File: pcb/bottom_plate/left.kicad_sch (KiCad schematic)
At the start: 18 parts

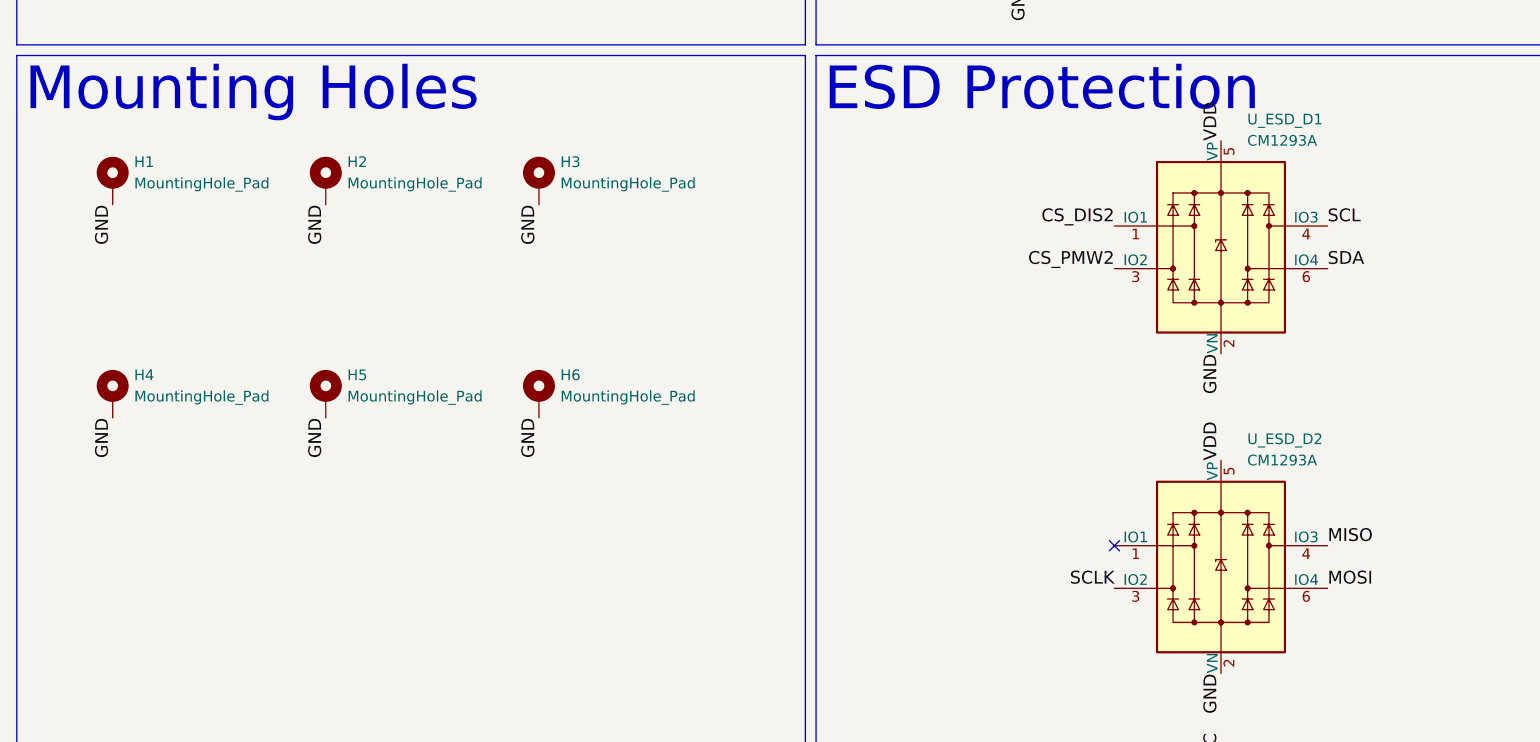
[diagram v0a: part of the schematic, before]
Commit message: Rework PCBs to ensure adequate clearance between them.
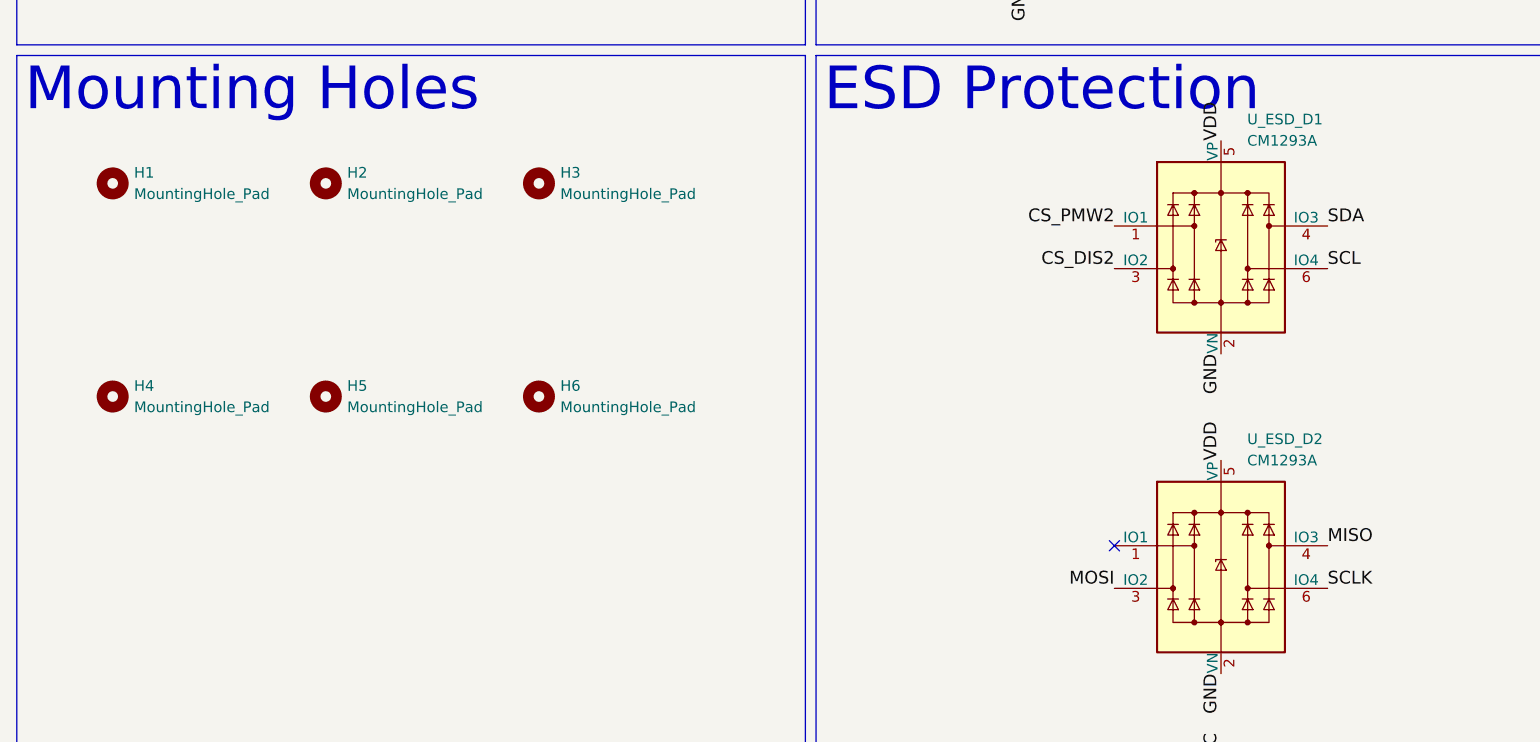
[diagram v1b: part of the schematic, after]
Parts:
- H1, H2, H3, H4, H5, H6: footprint MountingHole:MountingHole_2.2mm_M2_Pad -> MountingHole:MountingHole_2.2mm_M2; symbol Mechanical:MountingHole_Pad -> Mechanical:MountingHole
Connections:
- net CS_DIS2: now also U_ESD_D1.3 (IO2); no longer U_ESD_D1.1 (IO1)
- net CS_PMW2: now also U_ESD_D1.1 (IO1); no longer U_ESD_D1.3 (IO2)
- net GND: no longer H1.1, H2.1, H3.1, H4.1, H5.1, H6.1
- net MOSI: now also U_ESD_D2.3 (IO2); no longer U_ESD_D2.6 (IO4)
- net SCL: now also U_ESD_D1.6 (IO4); no longer U_ESD_D1.4 (IO3)
- net SCLK: now also U_ESD_D2.6 (IO4); no longer U_ESD_D2.3 (IO2)
- net SDA: now also U_ESD_D1.4 (IO3); no longer U_ESD_D1.6 (IO4)

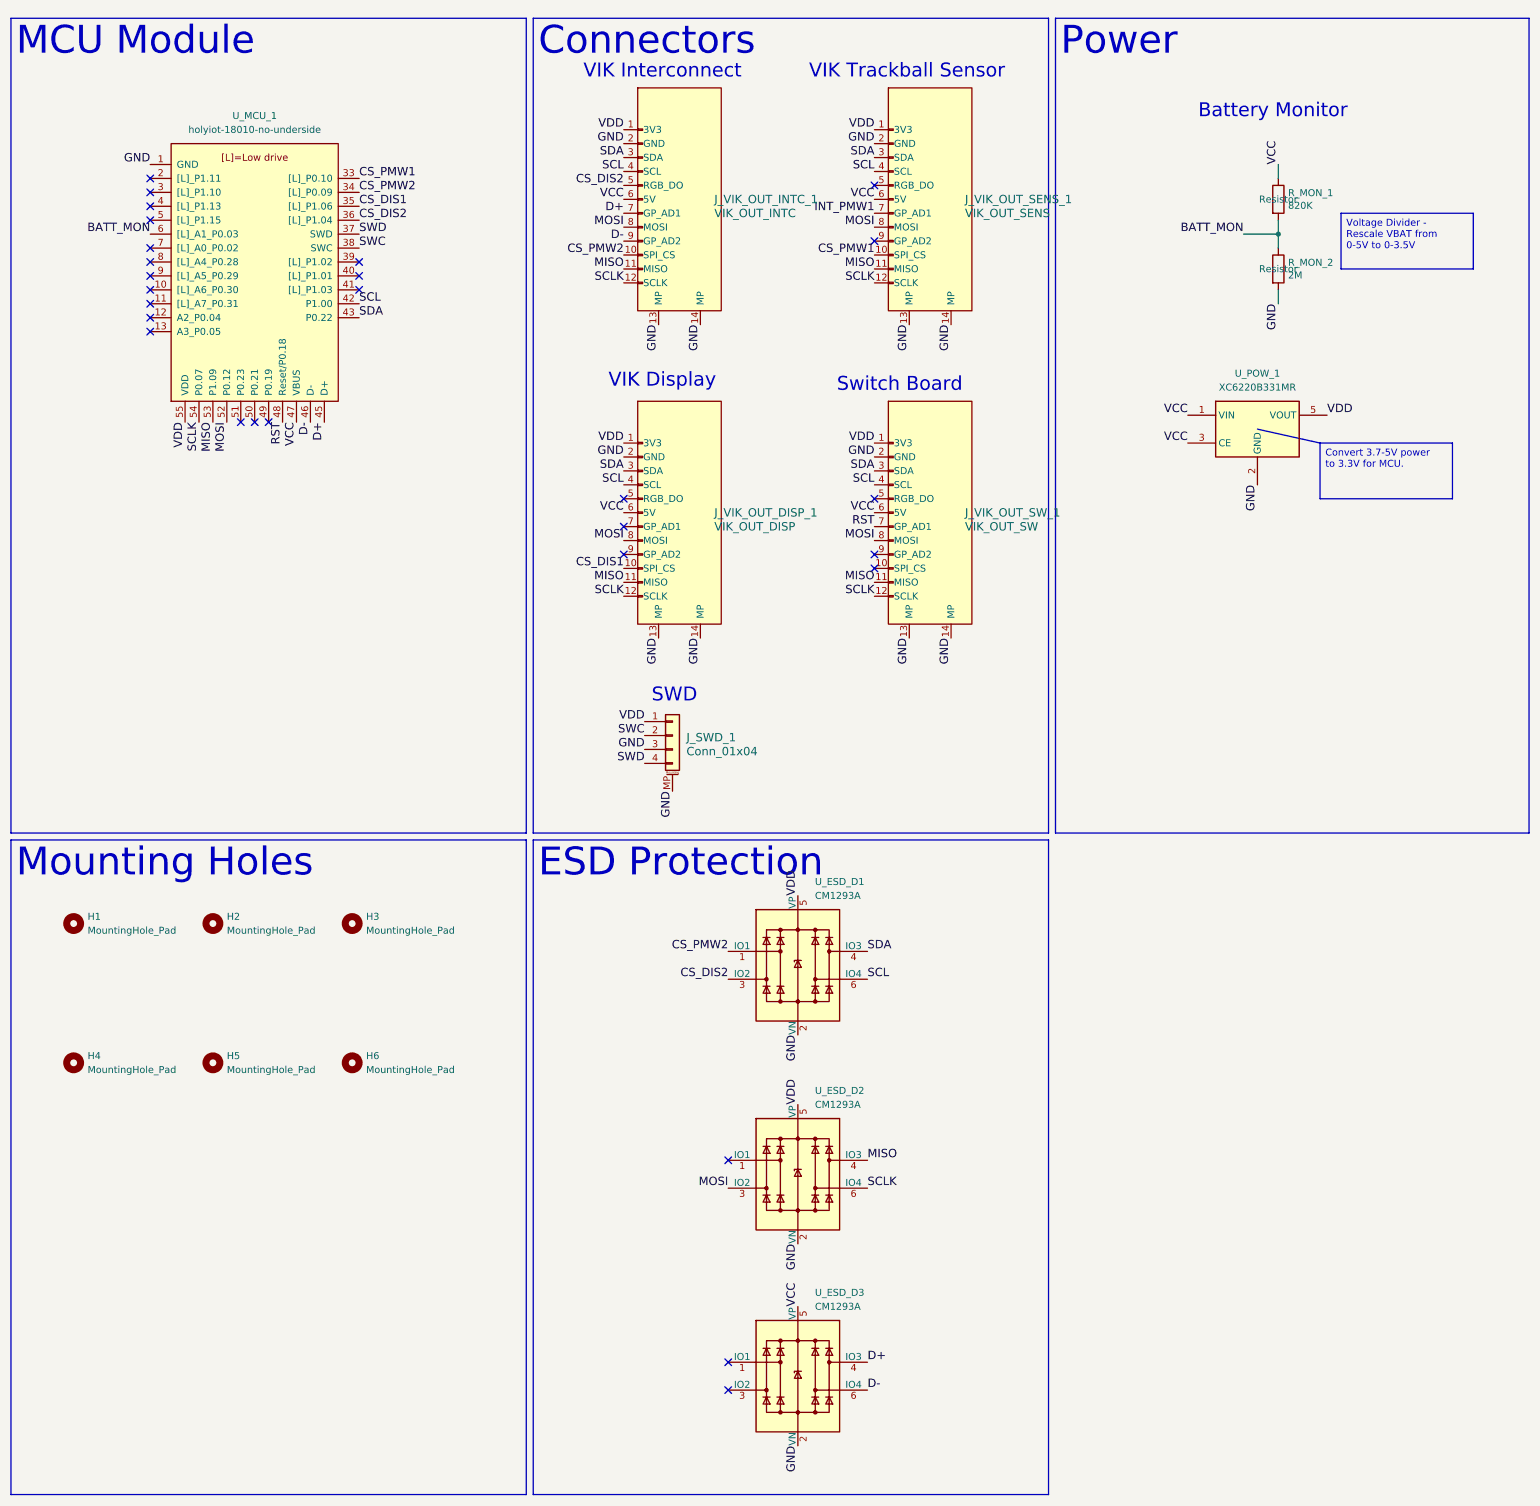
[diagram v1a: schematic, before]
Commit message: Remove redundant ESD protection from bottom plate.
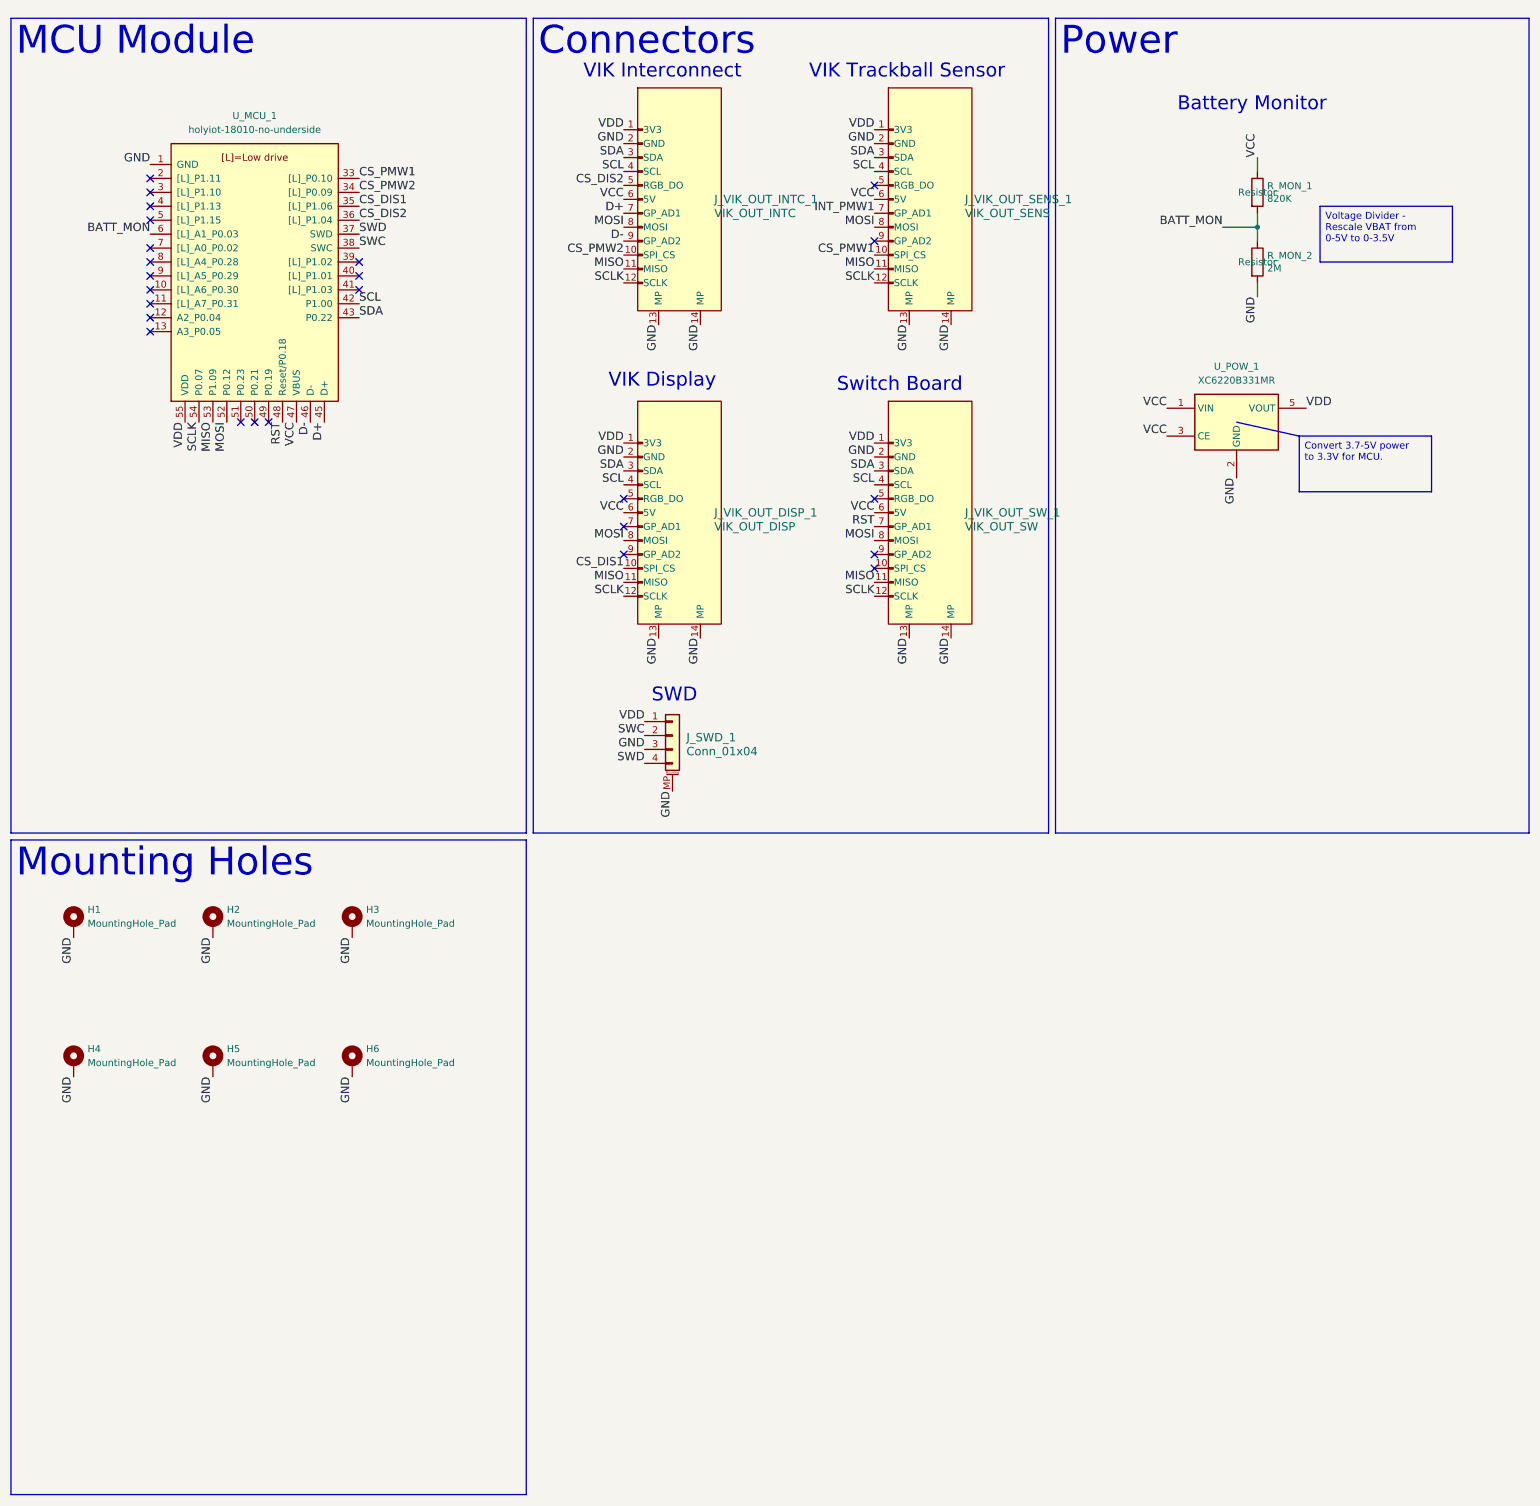
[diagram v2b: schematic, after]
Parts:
- removed U_ESD_D1, U_ESD_D2, U_ESD_D3: CM1293A, Package_TO_SOT_SMD:SOT-23-6, symbol Power_Protection:SRV05-4
- H1, H2, H3, H4, H5, H6: footprint MountingHole:MountingHole_2.2mm_M2 -> MountingHole:MountingHole_2.2mm_M2_Pad; symbol Mechanical:MountingHole -> Mechanical:MountingHole_Pad
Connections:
- net GND: now also H1.1, H2.1, H3.1, H4.1, H5.1, H6.1
- no-connect marks 28 -> 25
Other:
- moved on the sheet: R_MON_1, R_MON_2, U_POW_1

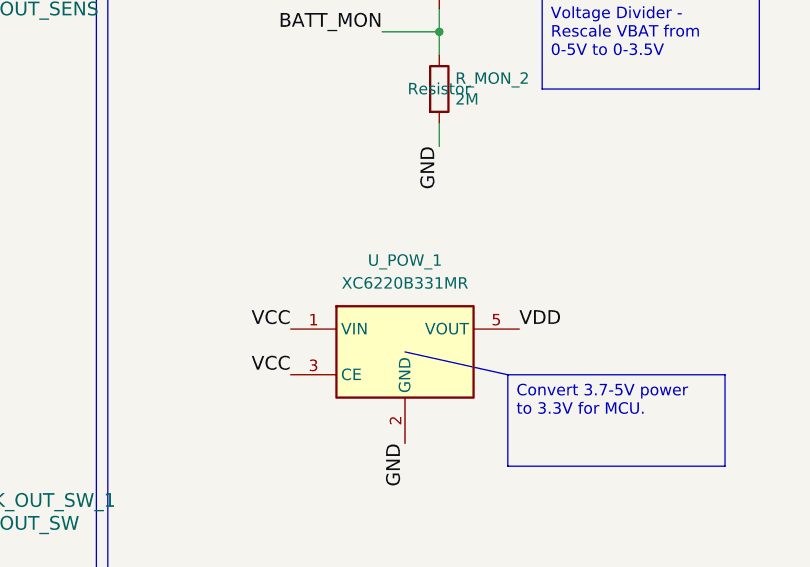
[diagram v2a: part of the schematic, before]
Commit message: Move all components to top of matrix plate to improve manufacturability.
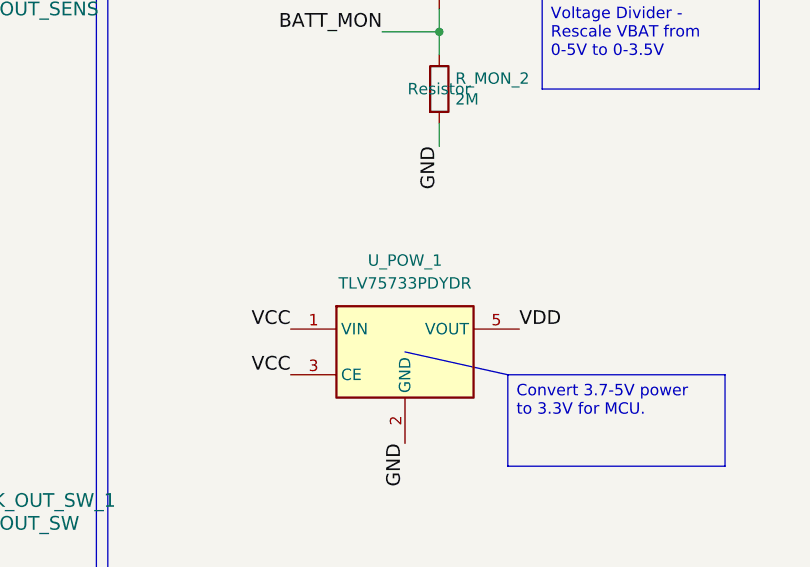
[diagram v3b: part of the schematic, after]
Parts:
- U_POW_1: value XC6220B331MR -> TLV75733PDYDR; LCSC (none) -> C22399950
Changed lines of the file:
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@@
 			)
 		)
-		(property "Value" "XC6220B331MR"
+		(property "Value" "TLV75733PDYDR"
 			(at 237.49 80.01 0)
 			(show_name no)
@@
 			(at 237.49 87.63 0)
 			(hide yes)
+			(show_name no)
+			(do_not_autoplace no)
+			(effects
+				(font
+					(size 1.27 1.27)
+				)
+			)
+		)
+		(property "LCSC" "C22399950"
+			(at 237.49 87.63 0)
+			(hide yes)

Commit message: Standardize on 0805 footprint for passive components.
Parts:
- R_MON_1, R_MON_2: footprint Resistor_SMD:R_1206_3216Metric_Pad1.30x1.75mm_HandSolder -> Resistor_SMD:R_0805_2012Metric_Pad1.20x1.40mm_HandSolder
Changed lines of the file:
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@@
 			)
 		)
-		(property "Footprint" "Resistor_SMD:R_1206_3216Metric_Pad1.30x1.75mm_HandSolder"
+		(property "Footprint" "Resistor_SMD:R_0805_2012Metric_Pad1.20x1.40mm_HandSolder"
 			(at 239.522 45.72 90)
 			(hide yes)
@@
 			)
 		)
-		(property "Footprint" "Resistor_SMD:R_1206_3216Metric_Pad1.30x1.75mm_HandSolder"
+		(property "Footprint" "Resistor_SMD:R_0805_2012Metric_Pad1.20x1.40mm_HandSolder"
 			(at 239.522 58.42 90)
 			(hide yes)
